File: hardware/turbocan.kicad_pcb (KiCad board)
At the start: 2 copper layers, 43 x 43 mm, 88 parts, among them J1 USB_C_Receptacle_USB2.0, J10 CAN_PORT, J11 FAN0, J12 FAN1, J13 HEAT, J14 PROBE, J2 STEPPER, J5 DEBUG, J7 ENDSTOPX, J8 ENDSTOPY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

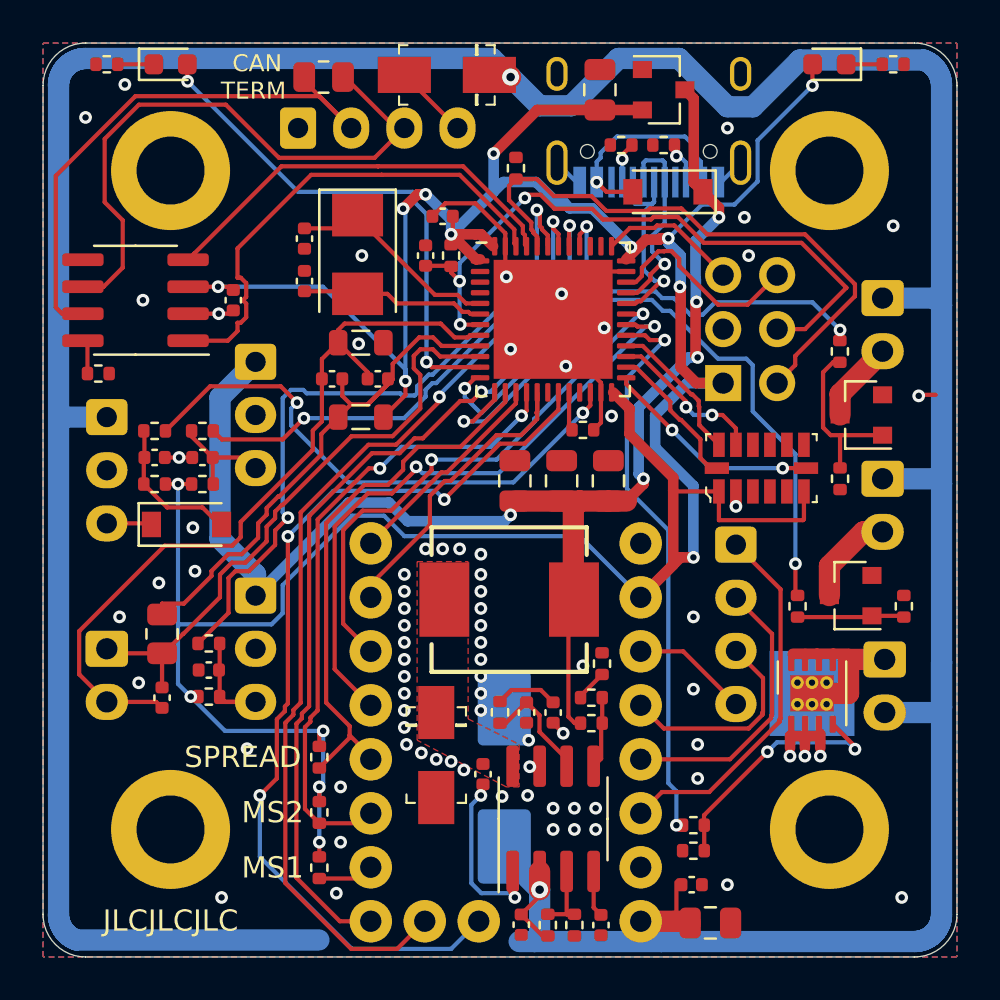
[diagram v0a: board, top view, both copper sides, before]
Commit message: Upgraded to KiCAD 6
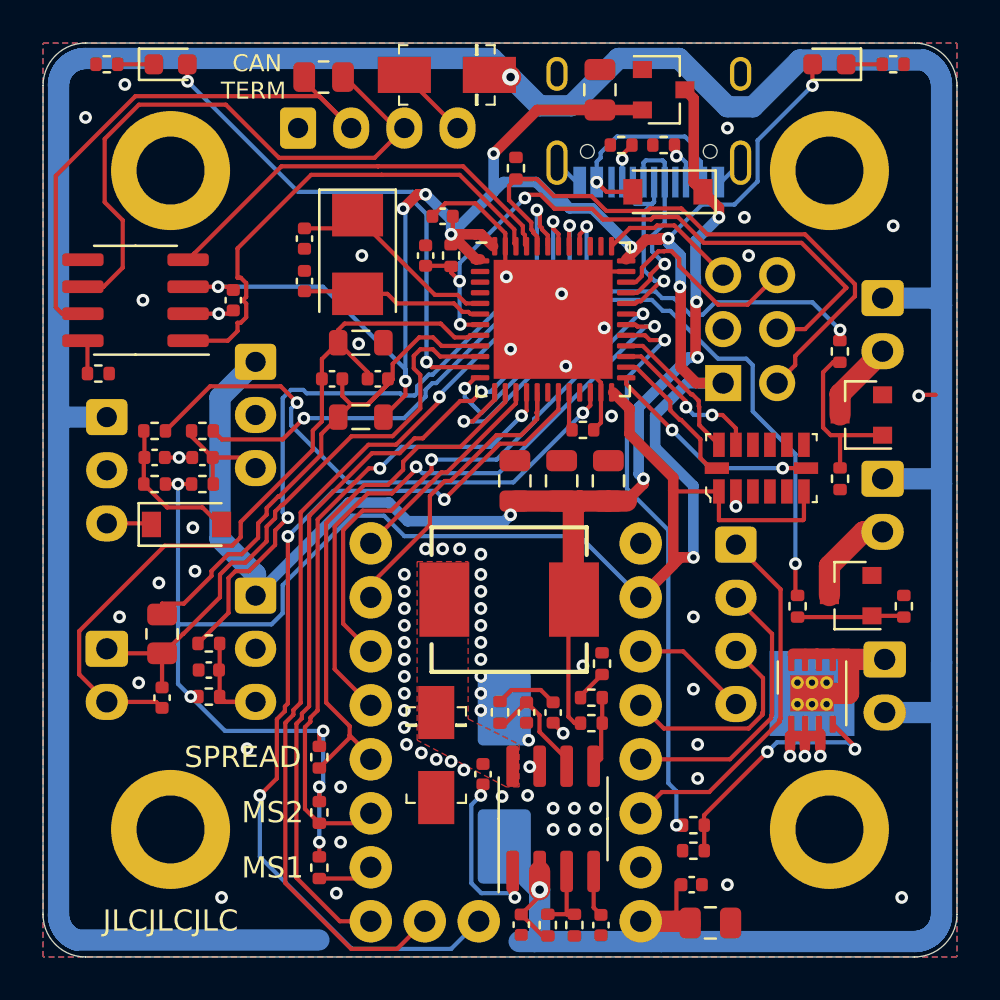
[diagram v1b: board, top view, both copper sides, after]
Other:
- net class 0.5mm removed
- net class 1mm removed
- net class Default removed

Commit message: First Test
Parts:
- removed H3: MountingHole, MountingHole:MountingHole_3.2mm_M3_DIN965_Pad
- removed R1: 5.1k, Resistor_SMD:R_0402_1005Metric
- removed R12, R13: 1k, Resistor_SMD:R_0402_1005Metric
- removed U9: ADXL345BCCZ, digikey-footprints:LGA-14_3x5mm_RevA
- added C24: 100nF, Capacitor_SMD:C_0402_1005Metric, F.Cu at (4.45, 12.7)
- added J15: SPI, Connector_JST:JST_XH_B6B-XH-A_1x06_P2.50mm_Vertical, F.Cu at (-20.8, 13.9)
- added J3: IO_PB10, Connector_JST:JST_XH_B3B-XH-A_1x03_P2.50mm_Vertical, F.Cu at (73.7, 30.5)
- J1: footprint Connector_USB:USB_C_Receptacle_HRO_TYPE-C-31-M-12 -> Connector_USB:USB_Micro-B_Amphenol_10118194_Horizontal; moved to F.Cu
- J7: value ENDSTOPX -> IO_PB6
- J8: value ENDSTOPY -> IO_PB7
- R2: value 5.1k -> 10k
- moved R2 56.0 mm to (-12.8, 20.4), turned to 0 degrees
- moved J14 39.5 mm to (54.5, 19.0), turned to 180 degrees
- moved J1 27.7 mm to (16.8, 26.7), turned to -90 degrees
- moved R3 23.8 mm to (35.1, 14.7)
- moved C1 23.5 mm to (60.5, 27.9)
- moved U1 23.5 mm to (63.5, 27.9)
- moved D1 21.3 mm to (22.9, 26.7)
- moved U3 15.1 mm to (30.2, 16.8), turned to 0 degrees
- moved D6 13.6 mm to (63.5, 20.3)
- moved R24 13.6 mm to (66.5, 20.3)
- moved D2 12.7 mm to (45.7, 15.5)
- moved R21 12.4 mm to (48.3, 22.9)
- moved R26 10.9 mm to (38.1, 15.7), turned to 90 degrees
- moved C3 9.78 mm to (25.9, 16.8), turned to 90 degrees
- moved J10 9.62 mm to (35.6, 18.3)
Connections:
- net CANH renamed Net-(R26-Pad1)
- net CANL renamed Net-(R26-Pad2)
- C10 pad 1: Net-(C10-Pad1) -> IO1
- C11 pad 1: Net-(C11-Pad1) -> IO2
- J7 pad 3: Net-(C10-Pad1) -> IO1
- J8 pad 3: Net-(C11-Pad1) -> IO2
- R2 pad 1: Net-(J1-PadB5) -> +3V3
- R2 pad 2: GND -> IO3
- R7 pad 2: Net-(C10-Pad1) -> IO1
- R8 pad 2: Net-(C11-Pad1) -> IO2
- U3 pad 5: (no net) -> unconnected-(U3-Pad5)
- U8 pad 18: (no net) -> unconnected-(U8-Pad18)
- U8 pad 2: (no net) -> unconnected-(U8-Pad2)
- U8 pad 21: (no net) -> IO3
- U8 pad 3: (no net) -> unconnected-(U8-Pad3)
- U8 pad 38: (no net) -> unconnected-(U8-Pad38)
- U8 pad 39: (no net) -> unconnected-(U8-Pad39)
- U8 pad 4: (no net) -> unconnected-(U8-Pad4)
- U8 pad 42: ENDSTOPX -> IO1
- U8 pad 43: ENDSTOPY -> IO2
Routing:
- net +24V: track 187.6 -> 93.7 mm, vias 2 -> 1
- net +3V3: track 163.8 -> 125.6 mm, vias 16 -> 13
- net ENDSTOPY: track 33.4 -> 0.00 mm, vias 2 -> 0
- net NRST: track 31.4 -> 5.02 mm, vias 3 -> 2
- net LED: track 24.5 -> 0.00 mm, vias 2 -> 0
- net ENDSTOPX: track 23.1 -> 0.00 mm, vias 2 -> 0
- net +5V: track 66.1 -> 44.8 mm, vias 5 -> 1
- net Net-(R26-Pad1): track 27.0 -> 7.39 mm
- net Net-(R26-Pad2): track 28.8 -> 15.3 mm
- net GND: track 31.8 -> 18.8 mm, vias 78 -> 0
- net A_CS: track 10.4 -> 0.00 mm, vias 2 -> 0
- net USBDP: track 9.78 -> 0.00 mm, vias 1 -> 0
- net USBDM: track 9.71 -> 0.00 mm, vias 1 -> 0
- net CANRX: track 19.8 -> 11.5 mm
- net A_MISO: track 7.49 -> 0.00 mm, vias 2 -> 0
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- removed copper zone on B.Cu, net GND
- removed copper zone on F.Cu, net GND
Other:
- board text removed: "DEBUG"
- board text removed: "FAN1"
- board text removed: "POWER"
- board text removed: "USB-C"

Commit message: Before DRC
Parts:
- removed H2: MountingHole, MountingHole:MountingHole_3.2mm_M3_DIN965_Pad
- removed J5: DEBUG, Connector_PinHeader_2.54mm:PinHeader_2x03_P2.54mm_Vertical
- added JP1: SolderJumper_2_Open, Jumper:SolderJumper-2_P1.3mm_Open_TrianglePad1.0x1.5mm, F.Cu at (25.4, 15.9)
- J1: value USB_C_Receptacle_USB2.0 -> USB_B_Micro_Receptacle_USB2.0
- J15: footprint Connector_JST:JST_XH_B6B-XH-A_1x06_P2.50mm_Vertical -> Connector_PinHeader_2.54mm:PinHeader_2x03_P2.54mm_Vertical; moved to B.Cu
- J3: moved to B.Cu
- R23: value 1k -> 10k
- moved J15 70.0 mm to (48.3, 24.8), turned to 180 degrees
- moved R24 58.8 mm to (19.7, 55.9)
- moved D6 58.4 mm to (17.1, 55.9)
- moved J3 56.8 mm to (17.1, 35.8)
- moved R23 54.2 mm to (54.0, 54.6), turned to 0 degrees
- moved D5 53.2 mm to (54.0, 55.9)
- moved R2 35.2 mm to (19.7, 33.9)
- moved C20 33.1 mm to (50.2, 21.6), turned to -90 degrees
- moved R27 32.4 mm to (48.9, 21.6), turned to 90 degrees
- moved D4 31.6 mm to (47.0, 19.1), turned to -90 degrees
- moved R28 29.4 mm to (46.8, 21.9), turned to 0 degrees
- moved C24 27.6 mm to (22.2, 33.9)
- moved R21 23.9 mm to (24.8, 18.4), turned to -90 degrees
- moved U1 21.1 mm to (43.2, 33.7), turned to -90 degrees
- moved C12 17.8 mm to (26.0, 28.1)
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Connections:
- net USBDM renamed USBDN
- C24 pad 2: unconnected-(C24-Pad2) -> GND
- D5 pad 2: LED -> +24V
- D6 pad 2: +3V3 -> +5V
- J13 pad 1: Net-(J13-Pad1) -> Net-(U7-Pad3)
- J15 pad 2: +5V -> A_MOSI
- J15 pad 3: A_CS -> A_SCK
- J15 pad 4: A_MOSI -> A_MISO
- J15 pad 5: A_MISO -> +5V
- J15 pad 6: A_SCK -> A_CS
- R2 pad 1: +3V3 -> +5V
- R23 pad 2: GND -> Net-(U7-Pad3)
- R7 pad 1: +3V3 -> +5V
- R8 pad 1: +3V3 -> +5V
- U7 pad 3: Net-(J13-Pad1) -> Net-(U7-Pad3)
- U8 pad 11: LED -> IO3
- U8 pad 21: IO3 -> unconnected-(U8-Pad21)
- U8 pad 22: PROBEZ -> unconnected-(U8-Pad22)
- U8 pad 38: unconnected-(U8-Pad38) -> PROBEZ
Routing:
- net +5V: track 44.8 -> 107.5 mm, vias 1 -> 5
- net IO2: track 3.46 -> 50.3 mm, vias 0 -> 1
- net IO1: track 2.74 -> 45.1 mm, vias 0 -> 1
- net USBDN: track 0.00 -> 34.2 mm, vias 0 -> 2
- net USBDP: track 0.00 -> 32.6 mm, vias 0 -> 2
- net Net-(U7-Pad3): track 0.00 -> 23.3 mm
- net GNDA: track 37.0 -> 14.1 mm
- net IO3: track 0.00 -> 19.3 mm, vias 0 -> 2
- net PROBEZ: track 25.9 -> 6.94 mm, vias 2 -> 0
- net INDEX: track 44.6 -> 30.4 mm, vias 3 -> 0
- net VDDA: track 23.9 -> 11.0 mm
- net SWDIO: track 9.75 -> 0.00 mm
- net TH0: track 27.3 -> 19.0 mm
- net A_SCK: track 0.00 -> 8.12 mm
- net Net-(J13-Pad1): track 7.83 -> 0.00 mm
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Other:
- board text added: "TurboCAN v0.3"
- board text removed: "24V"
- board text removed: "3.3V"
- board text removed: "ACTIVITY"
- board text removed: "BT0"
- board text removed: "CAN"
- board text removed: "RST"
- board text removed: "SWC"
- board text removed: "SWIO"
- board text removed: "TH"
- board text removed: "TurboCAN v0.2"
- board text removed: "X"
- board text removed: "Z"
- board text removed: "←FAN0"

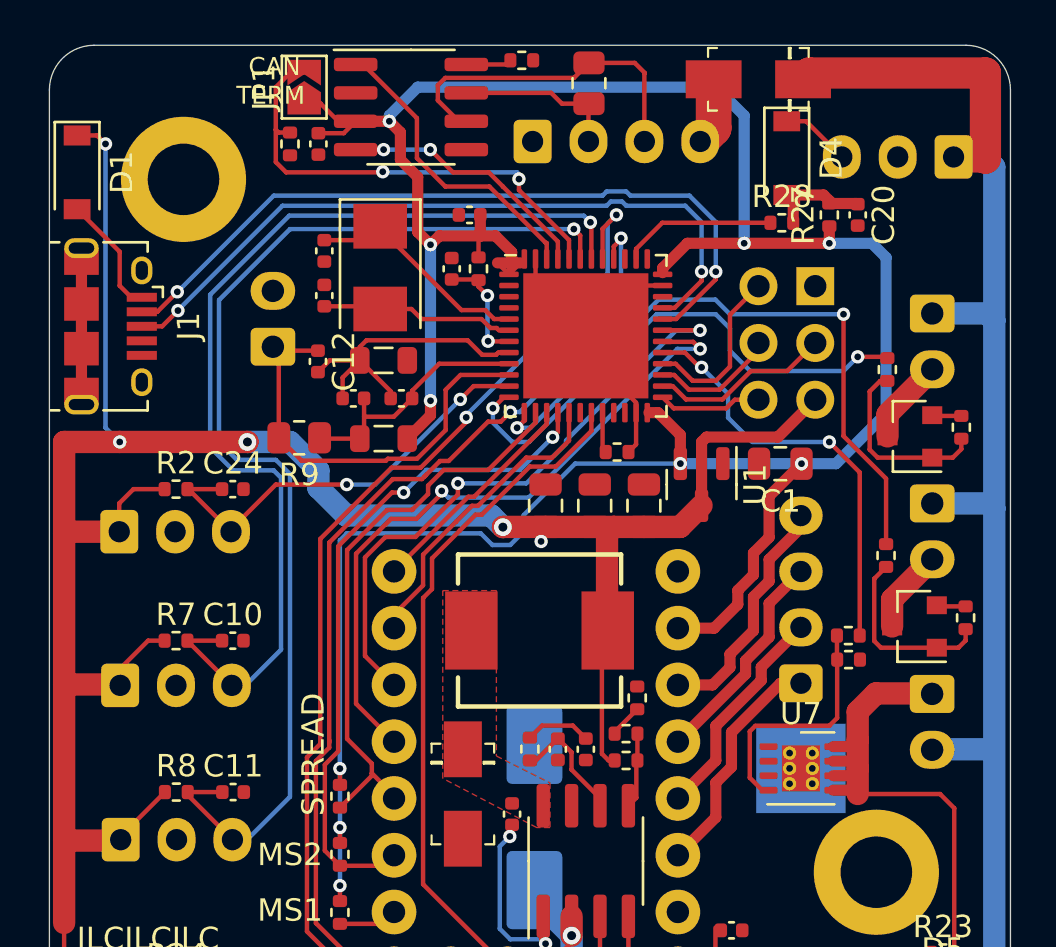
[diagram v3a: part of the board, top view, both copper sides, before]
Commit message: Fixed violations, still have more DRC.
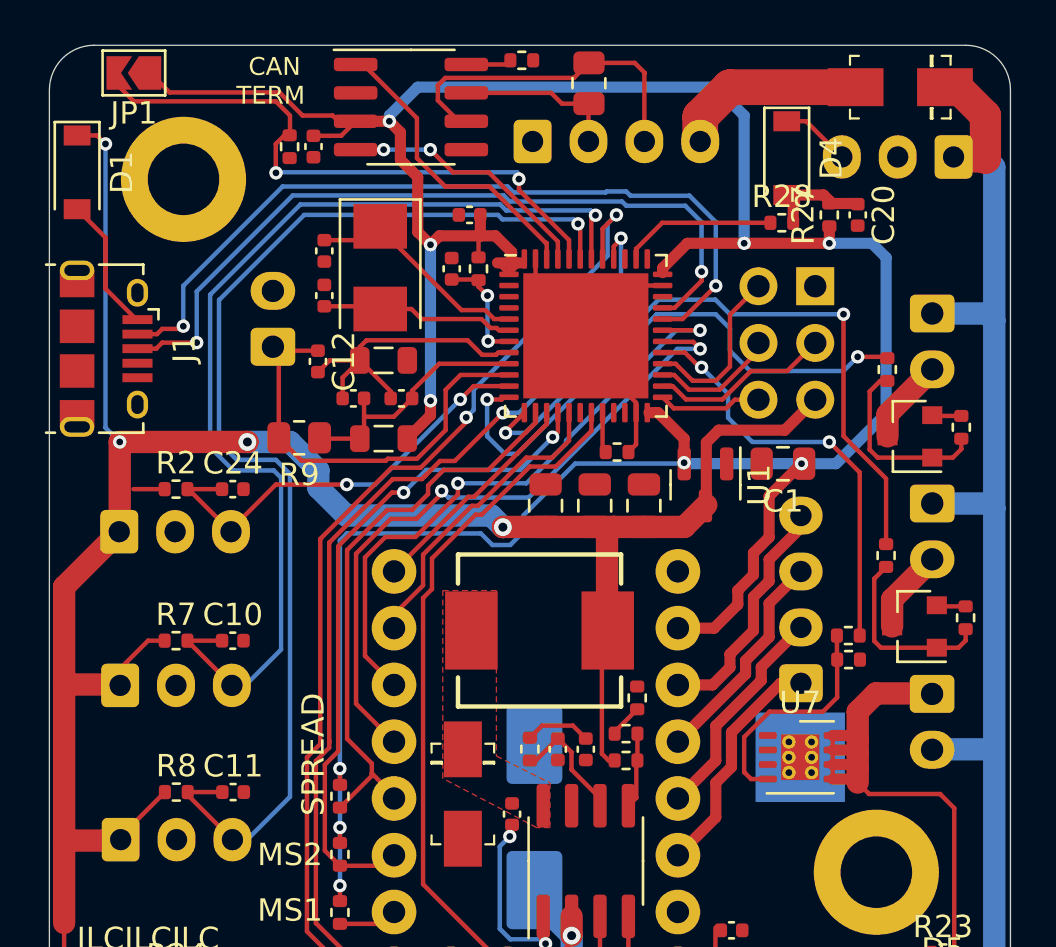
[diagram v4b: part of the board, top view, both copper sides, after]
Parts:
- moved JP1 7.65 mm to (17.8, 15.2), turned to 180 degrees
- moved D2 6.36 mm to (52.1, 15.9)
- moved J1 1.02 mm to (16.5, 27.6)
- moved U7 0.50 mm to (47.6, 45.9)
- moved C3 0.25 mm to (25.8, 18.5)
- moved U1 0.17 mm to (43.4, 33.7)
- moved R21 0.12 mm to (24.7, 18.5)
- moved C1 0.12 mm to (46.8, 32.7)
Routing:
- net +24V: track 94.9 -> 87.0 mm
- net +3V3: track 131.0 -> 138.8 mm
- net +5V: track 107.5 -> 100.9 mm, vias 5 -> 4
- net BOOT0: track 20.9 -> 27.3 mm
- net GND: track 16.2 -> 10.4 mm
- net Net-(D2-PadA): track 3.03 -> 8.60 mm
- net USBDP: track 32.6 -> 34.8 mm
- net USBDN: track 34.2 -> 36.2 mm
- net Net-(U7-Pad3): track 23.3 -> 24.9 mm
- net FAN0: track 23.5 -> 25.1 mm
- net Net-(D1-Pad2): track 4.94 -> 6.08 mm
- net FAN1: track 29.1 -> 30.2 mm
- net IO1: track 45.1 -> 46.0 mm
- net IO2: track 50.3 -> 51.1 mm

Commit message: First Manufacturing Upload
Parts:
- added REF**: VoronLogo, turbocan:VoronLogo, B.Cu at (35.9, 26.6)
- moved D1 0.97 mm to (15.2, 20.7)
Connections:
- J1 pad 6: GND -> unconnected-(J1-Pad6)
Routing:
- net GND: track 10.4 -> 38.4 mm, vias 0 -> 105
- net Net-(U7-Pad3): track 24.9 -> 31.0 mm
- net GNDA: track 14.1 -> 19.3 mm
- net Net-(R16-Pad1): track 10.4 -> 12.3 mm, vias 0 -> 2
- net IO1: track 46.0 -> 44.4 mm
- net +5V: track 100.9 -> 102.4 mm
- net IO2: track 51.1 -> 49.7 mm
- net CANTX: track 13.3 -> 14.1 mm
- net CANRX: track 11.5 -> 12.3 mm
- net +24V: track 87.0 -> 86.5 mm
- added copper zone on B.Cu, net GND
- added copper zone on F.Cu, net GND
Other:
- board text added: "24V"
- board text added: "BOOT0"
- board text added: "FAN0/PA2"
- board text added: "FAN1/PA3"
- board text added: "H"
- board text added: "HEAT/PA8"
- board text added: "L"
- board text added: "PA1"
- board text added: "PB6"
- board text added: "PB7"
- board text added: "PROBEZ"
- board text added: "PROBEZ /PA15"
- board text added: "PWR"
- board text added: "TH/PA0"
- board text added: "TH0 R >"
- board text added: "TurboCAN v0.3.0"
- board text removed: "TurboCAN v0.3"
- board text removed: "Y"
